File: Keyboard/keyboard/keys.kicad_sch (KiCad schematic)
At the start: 26 parts, among them SW10 Cherry_MX_1u, SW11 Cherry_MX_1u, SW12 Cherry_MX_1u, SW13 Cherry_MX_1u, SW2 Cherry_MX_1u, SW3 Cherry_MX_1u, SW4 Cherry_MX_1u, SW5 Cherry_MX_1u, SW6 Cherry_MX_1u, SW7 Cherry_MX_1u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

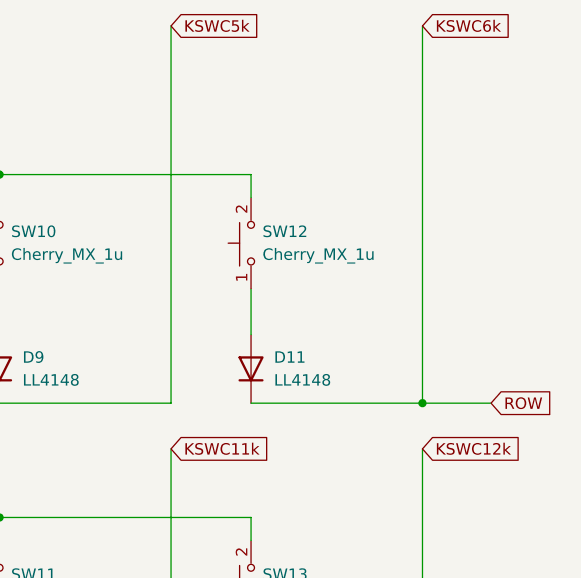
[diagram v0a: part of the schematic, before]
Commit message: fixing keyboard and pot project schematics
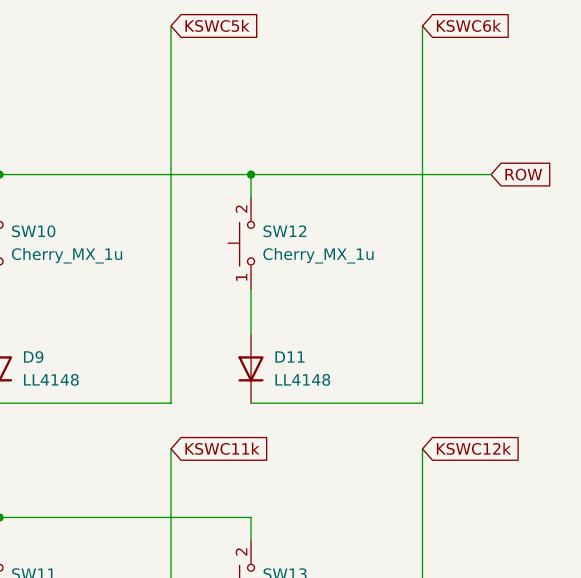
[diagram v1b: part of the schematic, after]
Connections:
- net KSWC6k: no longer SW11.2, SW13.2, SW3.2, SW5.2, SW7.2, SW9.2
- net ROW: now reaches R4.2, SW10.2, SW12.2, SW2.2, SW4.2, SW6.2, SW8.2
- net ROW: now also SW11.2, SW13.2, SW3.2, SW5.2, SW7.2, SW9.2
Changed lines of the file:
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@@
 (kicad_sch (version 20211123) (generator eeschema)
   (paper "A4")
+  (junction (at 247.65 53.34) (diameter 0) (color 0 0 0 0)
+  )
   (junction (at 31.75 53.34) (diameter 0) (color 0 0 0 0)
   )
   (junction (at 86.36 53.34) (diameter 0) (color 0 0 0 0)
   )
-  (junction (at 266.7 78.74) (diameter 0) (color 0 0 0 0)
-  )
   (junction (at 44.45 91.44) (diameter 0) (color 0 0 0 0)
   )
@@
     (stroke (width 0) (type default) (color 0 0 0 0))
   )
-  (wire (pts (xy 266.7 78.74) (xy 274.32 78.74))
-    (stroke (width 0) (type default) (color 0 0 0 0))
-  )
   (wire (pts (xy 247.65 78.74) (xy 266.7 78.74))
+    (stroke (width 0) (type default) (color 0 0 0 0))
+  )
+  (wire (pts (xy 274.32 53.34) (xy 247.65 53.34))
     (stroke (width 0) (type default) (color 0 0 0 0))
   )
@@
     )
   )
-  (global_label "ROW" (shape input) (at 274.32 78.74 0) (fields_autoplaced)
-    (effects (font (size 1.27 1.27)) (justify left))
-    (property "Intersheet References" "${INTERSHEET_REFS}" (id 0) (at 280.785 78.8194 0)
-      (effects (font (size 1.27 1.27)) (justify left) hide)
-    )
+  (global_label "ROW" (shape input) (at 274.32 53.34 0) (fields_autoplaced)
+    (effects (font (size 1.27 1.27)) (justify left))
+    (property "Intersheet References" "${INTERSHEET_REFS}" (id 0) (at 280.785 53.4194 0)
+      (effects (font (size 1.27 1.27)) (justify left) hide)
+    )

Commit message: pcb design fixing
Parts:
- removed D1, D10, D11, D12, D2, D3, D4, D5, D6, D7, D8, D9: LL4148, Diode_SMD:D_MiniMELF, symbol Diode:LL4148
- removed R3, R4: 10K, Resistor_SMD:R_0805_2012Metric_Pad1.20x1.40mm_HandSolder, symbol Device:R
- added R10, R13, R14, R17, R18, R21, R22, R25, R26, R29, R30, R9: 10K, Resistor_SMD:R_0805_2012Metric_Pad1.20x1.40mm_HandSolder, symbol Device:R
- added R11, R12, R15, R16, R19, R20, R23, R24, R27, R28, R31, R32: 100, Resistor_SMD:R_0805_2012Metric_Pad1.20x1.40mm_HandSolder, symbol Device:R
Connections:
- net +3V3: now also R10.2, R13.2, R14.2, R17.2, R18.2, R21.2, R22.2, R25.2, R26.2, R29.2, R30.2, R9.2
- net KSWC10k: now also R22.1, R24.1
- net KSWC11k: now also R26.1, R28.1
- net KSWC12k: now also R30.1, R32.1
- net KSWC1k: now also R11.1, R9.1
- net KSWC2k: now also R13.1, R16.1
- net KSWC3k: now also R17.1, R19.1
- net KSWC4k: now also R21.1, R23.1
- net KSWC5k: now also R25.1, R27.1
- net KSWC6k: now also R29.1, R31.1
- net KSWC7k: now also R10.1, R12.1
- net KSWC8k: now also R14.1, R15.1
- net KSWC9k: now also R18.1, R20.1
- net GND: now reaches SW9.1
- net GND: now also SW10.1, SW11.1, SW12.1, SW13.1, SW2.1, SW3.1, SW4.1, SW5.1, SW6.1, SW7.1, SW8.1
- removed net ROW: SW10.2, SW11.2, SW12.2, SW13.2, SW2.2, SW3.2, SW4.2, SW5.2, SW6.2, SW7.2, SW8.2, SW9.2
- new net: R32.2, SW13.2
- new net: R16.2, SW4.2
- new net: R19.2, SW6.2
- new net: R11.2, SW2.2
- new net: R27.2, SW10.2
- new net: R12.2, SW3.2
- new net: R31.2, SW12.2
- new net: R20.2, SW7.2
- new net: R23.2, SW8.2
- new net: R15.2, SW5.2
- new net: R24.2, SW9.2
- new net: R28.2, SW11.2

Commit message: gerber files generated
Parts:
- added H1, H2, H3, H4, H5, H6: MountingHole, MountingHole:MountingHole_3.2mm_M3_Pad_Via, symbol Mechanical:MountingHole
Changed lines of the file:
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@@
     (pin "2")
+  )
+  (symbol (lib_id "Mechanical:MountingHole") (at 91.44 161.29 0) (unit 1)
+    (in_bom yes) (on_board yes) (fields_autoplaced)
+    (property "Reference" "H6" (id 0) (at 93.98 160.0199 0)
+      (effects (font (size 1.27 1.27)) (justify left))
+    )
+    (property "Value" "MountingHole" (id 1) (at 93.98 162.5599 0)
+      (effects (font (size 1.27 1.27)) (justify left))
+    )
+    (property "Footprint" "MountingHole:MountingHole_3.2mm_M3_Pad_Via" (id 2) (at 91.44 161.29 0)
+      (effects (font (size 1.27 1.27)) hide)
+    )
+    (property "Datasheet" "~" (id 3) (at 91.44 161.29 0)
+      (effects (font (size 1.27 1.27)) hide)
+    )
   )
   (symbol (lib_id "power:GND") (at 218.44 121.92 0) (unit 1)
@@
     )
     (pin "1")
+  )
+  (symbol (lib_id "Mechanical:MountingHole") (at 30.48 161.29 0) (unit 1)
+    (in_bom yes) (on_board yes) (fields_autoplaced)
+    (property "Reference" "H2" (id 0) (at 33.02 160.0199 0)
+      (effects (font (size 1.27 1.27)) (justify left))
+    )
+    (property "Value" "MountingHole" (id 1) (at 33.02 162.5599 0)
+      (effects (font (size 1.27 1.27)) (justify left))
+    )
+    (property "Footprint" "MountingHole:MountingHole_3.2mm_M3_Pad_Via" (id 2) (at 30.48 161.29 0)
+      (effects (font (size 1.27 1.27)) hide)
+    )
+    (property "Datasheet" "~" (id 3) (at 30.48 161.29 0)
+      (effects (font (size 1.27 1.27)) hide)
+    )
   )
   (symbol (lib_id "Device:R") (at 97.79 38.1 90) (unit 1)
@@
     (pin "2")
   )
+  (symbol (lib_id "Mechanical:MountingHole") (at 30.48 149.86 0) (unit 1)
+    (in_bom yes) (on_board yes) (fields_autoplaced)
+    (property "Reference" "H1" (id 0) (at 33.02 148.5899 0)
+      (effects (font (size 1.27 1.27)) (justify left))
+    )
+    (property "Value" "MountingHole" (id 1) (at 33.02 151.1299 0)
+      (effects (font (size 1.27 1.27)) (justify left))
+    )
+    (property "Footprint" "MountingHole:MountingHole_3.2mm_M3_Pad_Via" (id 2) (at 30.48 149.86 0)
+      (effects (font (size 1.27 1.27)) hide)
+    )
+    (property "Datasheet" "~" (id 3) (at 30.48 149.86 0)
+      (effects (font (size 1.27 1.27)) hide)
+    )
+  )
   (symbol (lib_id "Device:R") (at 135.89 38.1 90) (unit 1)
     (in_bom yes) (on_board yes)
@@
     (pin "2")
   )
+  (symbol (lib_id "Mechanical:MountingHole") (at 60.96 149.86 0) (unit 1)
+    (in_bom yes) (on_board yes) (fields_autoplaced)
+    (property "Reference" "H3" (id 0) (at 63.5 148.5899 0)
+      (effects (font (size 1.27 1.27)) (justify left))
+    )
+    (property "Value" "MountingHole" (id 1) (at 63.5 151.1299 0)
+      (effects (font (size 1.27 1.27)) (justify left))
+    )
+    (property "Footprint" "MountingHole:MountingHole_3.2mm_M3_Pad_Via" (id 2) (at 60.96 149.86 0)
+      (effects (font (size 1.27 1.27)) hide)
+    )
+    (property "Datasheet" "~" (id 3) (at 60.96 149.86 0)
+      (effects (font (size 1.27 1.27)) hide)
+    )
+  )
   (symbol (lib_id "cherry_mx:Cherry_MX_1u") (at 142.24 113.03 90) (unit 1)
     (in_bom yes) (on_board yes) (fields_autoplaced)
@@
     (pin "1")
   )
+  (symbol (lib_id "Mechanical:MountingHole") (at 60.96 161.29 0) (unit 1)
+    (in_bom yes) (on_board yes) (fields_autoplaced)
+    (property "Reference" "H4" (id 0) (at 63.5 160.0199 0)
+      (effects (font (size 1.27 1.27)) (justify left))
+    )
+    (property "Value" "MountingHole" (id 1) (at 63.5 162.5599 0)
+      (effects (font (size 1.27 1.27)) (justify left))
+    )
+    (property "Footprint" "MountingHole:MountingHole_3.2mm_M3_Pad_Via" (id 2) (at 60.96 161.29 0)
+      (effects (font (size 1.27 1.27)) hide)
+    )
+    (property "Datasheet" "~" (id 3) (at 60.96 161.29 0)
+      (effects (font (size 1.27 1.27)) hide)
+    )
+  )
   (symbol (lib_id "Device:R") (at 203.2 31.75 180) (unit 1)
     (in_bom yes) (on_board yes) (fields_autoplaced)
@@
     (pin "2")
   )
+  (symbol (lib_id "Mechanical:MountingHole") (at 91.44 149.86 0) (unit 1)
+    (in_bom yes) (on_board yes) (fields_autoplaced)
+    (property "Reference" "H5" (id 0) (at 93.98 148.5899 0)
+      (effects (font (size 1.27 1.27)) (justify left))
+    )
+    (property "Value" "MountingHole" (id 1) (at 93.98 151.1299 0)
+      (effects (font (size 1.27 1.27)) (justify left))
+    )
+    (property "Footprint" "MountingHole:MountingHole_3.2mm_M3_Pad_Via" (id 2) (at 91.44 149.86 0)
+      (effects (font (size 1.27 1.27)) hide)
+    )
+    (property "Datasheet" "~" (id 3) (at 91.44 149.86 0)
+      (effects (font (size 1.27 1.27)) hide)
+    )
+  )
   (symbol (lib_id "cherry_mx:Cherry_MX_1u") (at 218.44 113.03 90) (unit 1)
